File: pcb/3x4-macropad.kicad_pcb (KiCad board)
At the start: 2 copper layers, 83.1 x 78.9 mm, 47 parts, among them SW1 SW_Push, SW10 SW_Push, SW11 SW_Push, SW12 SW_Push, SW2 SW_Push, SW3 SW_Push, SW4 SW_Push, SW5 SW_Push, SW6 SW_Push, SW7 SW_Push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

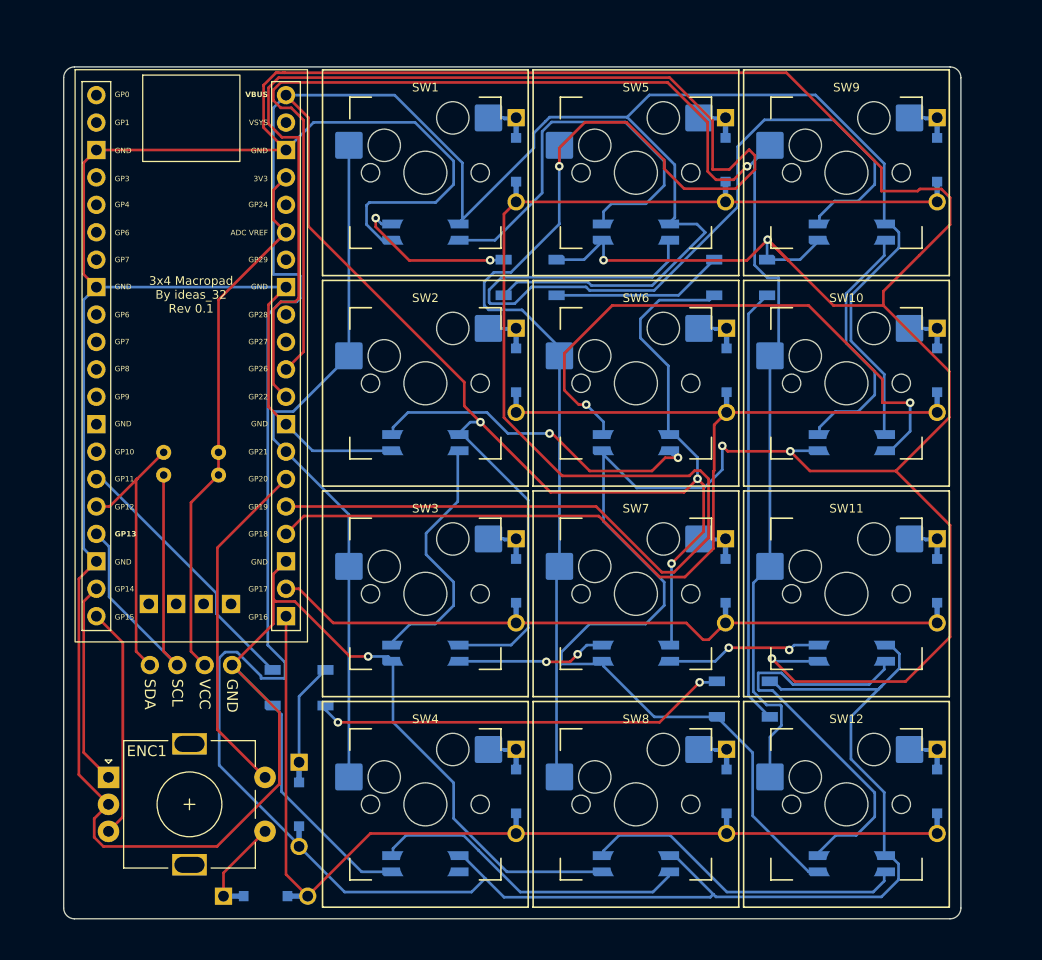
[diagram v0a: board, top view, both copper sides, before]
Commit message: Updated README.md and pcb with jlcpcb clearance requirements
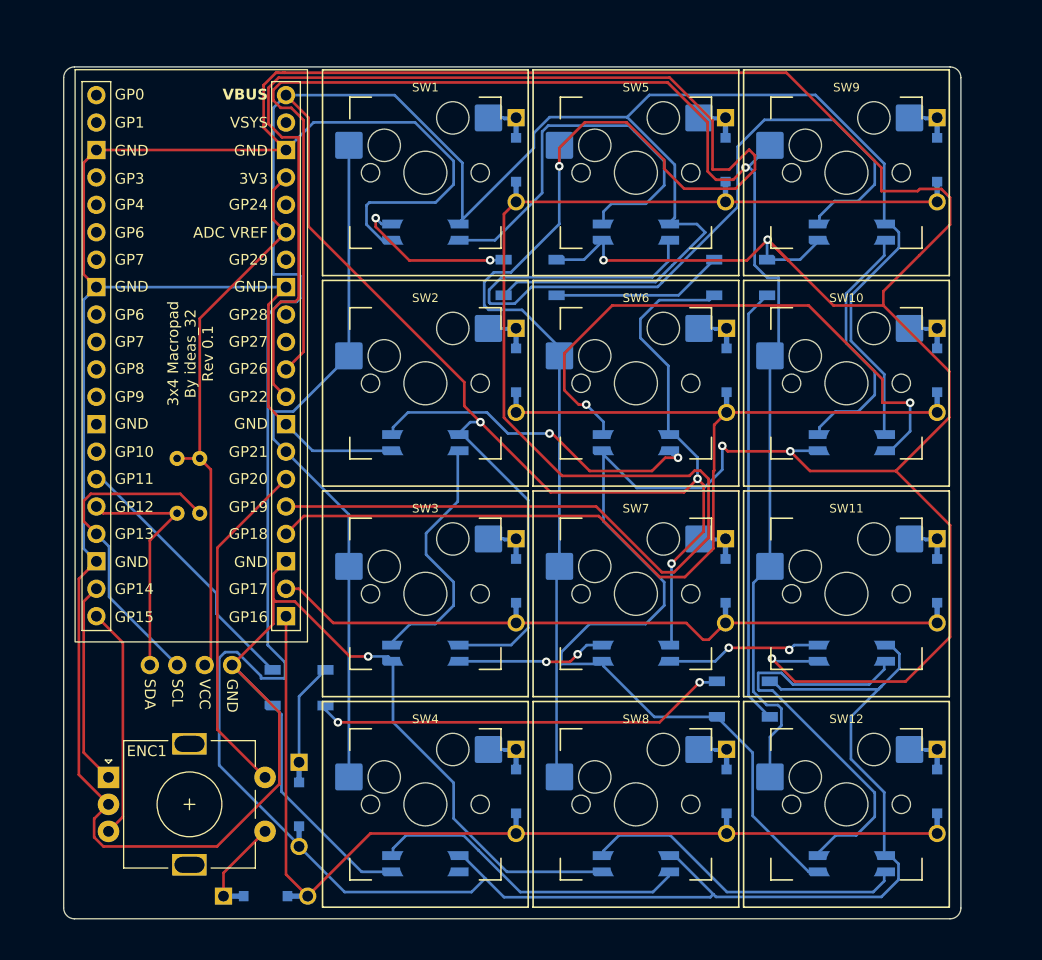
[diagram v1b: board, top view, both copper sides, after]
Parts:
- moved R1 5.77 mm to (138.0, 72.5), turned to 90 degrees
- moved R2 4.87 mm to (140.1, 72.5), turned to 90 degrees
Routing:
- net OLED_SDA: track 26.2 -> 22.8 mm
- net OLED_SCL: track 33.4 -> 30.6 mm
- net VCC: track 50.3 -> 52.2 mm
- net COL3: track 145.3 -> 143.9 mm

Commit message: stuff
- cleaned up routing
- changed per-key rgb footprint
- changed resistor footprint
- changed diode footprint to actually support sod123
- made power traces 0.5mm
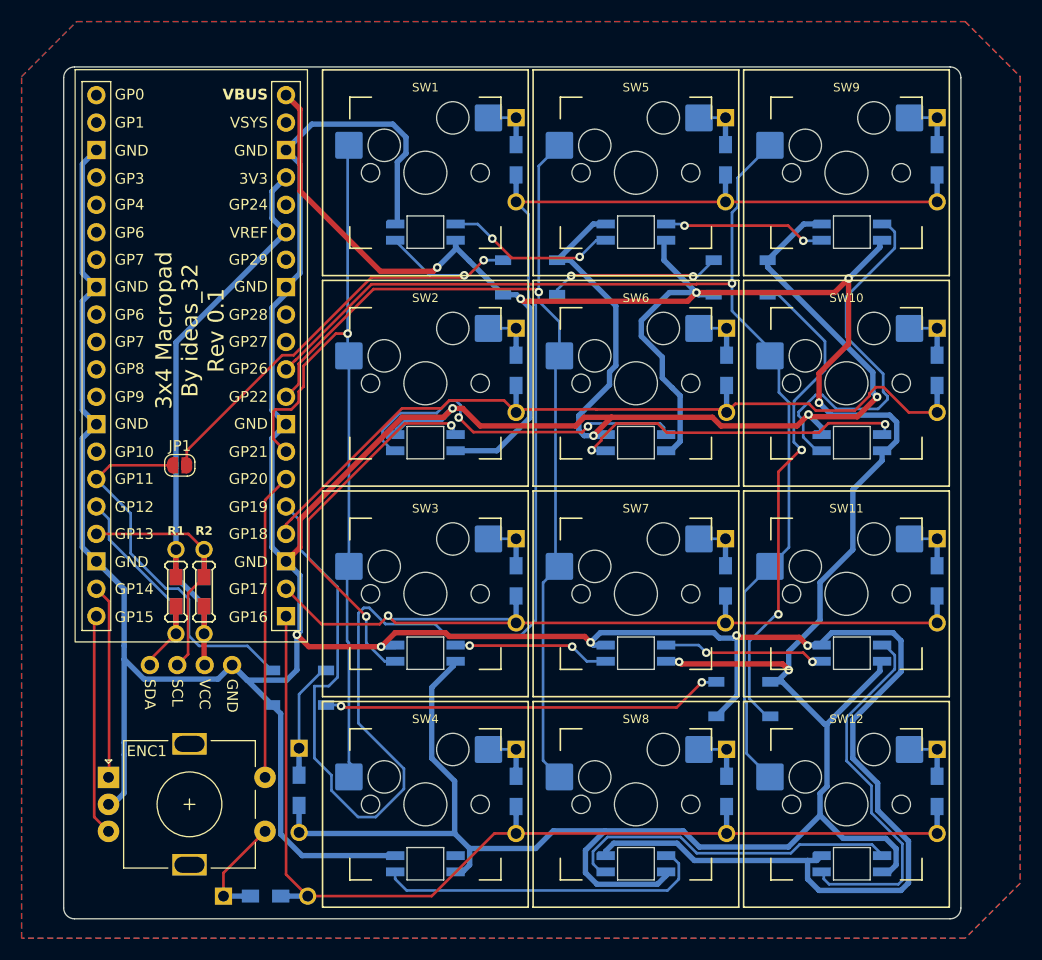
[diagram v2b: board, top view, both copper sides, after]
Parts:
- removed D18: D_Small, Keebio-Parts:Diode-dual
- added D14: 1N4148, Keebio-Parts:Diode-Hybrid-Back, B.Cu at (149.3, 98.2)
- added JP1: SolderJumper_2_Open, Jumper:SolderJumper-2_P1.3mm_Open_RoundedPad1.0x1.5mm, F.Cu at (138.2, 68.1)
- D1, D10, D11, D12, D13, D2, D3, D4, D5, D6, D7, D8, D9: value D_Small -> 1N4148; footprint Keebio-Parts:Diode-dual -> Keebio-Parts:Diode-Hybrid-Back
- LED1, LED10, LED11, LED12, LED2, LED3, LED4, LED5, LED6, LED7, LED8, LED9: footprint SK6812MINI-E:SK6812MINIE -> Keebio-Parts:SK6812-MINI-E
- LED13, LED14, LED15, LED16: footprint LED_SMD:LED_WS2812B_PLCC4_5.0x5.0mm_P3.2mm -> Keebio-Parts:WS2812B
- R1, R2: footprint Resistor_THT:R_Axial_DIN0204_L3.6mm_D1.6mm_P5.08mm_Horizontal -> Keebio-Parts:Resistor-Hybrid
- U1: value WeAct RP2040 Pico -> WeAct-RP2040-Pico
- moved R2 7.27 mm to (140.5, 79.8)
- moved R1 7.26 mm to (137.9, 79.8), turned to -90 degrees
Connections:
- U1 pad 13: unconnected-(U1-GND-Pad13) -> GND
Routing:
- net VBUS: track 467.7 -> 302.8 mm, vias 3 -> 7
- net GND: track 576.9 -> 444.5 mm, vias 6 -> 9
- net COL2: track 178.7 -> 89.4 mm
- net Net-(LED10-DIN): track 77.7 -> 15.4 mm, vias 0 -> 2
- net COL3: track 143.9 -> 107.6 mm
- net Net-(JP1-B): track 15.8 -> 45.4 mm
- net ROW1: track 101.4 -> 72.7 mm
- net ROW0: track 135.2 -> 158.4 mm
- net Net-(LED8-DIN): track 54.1 -> 31.3 mm
- net Net-(LED11-DIN): track 38.2 -> 16.3 mm, vias 0 -> 2
- net Net-(LED6-DIN): track 24.0 -> 35.1 mm, vias 0 -> 2
- net OLED_SCL: track 30.6 -> 19.7 mm
- net RGB: track 24.8 -> 35.4 mm
- net Net-(LED10-DOUT): track 23.9 -> 34.1 mm
- net ROW2: track 68.5 -> 78.6 mm, vias 0 -> 1
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- added copper zone on B.Cu, net GND
- added copper zone on F.Cu, net GND
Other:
- board text added: "COL0"
- board text added: "COL1"
- board text added: "COL2"
- board text added: "COL3"
- board text added: "ENC A"
- board text added: "ENC B"
- board text added: "GND"
- board text added: "Pins not labeled are unused"
- board text added: "RGB"
- board text added: "ROW0"
- board text added: "ROW1"
- board text added: "ROW2"
- board text added: "ROW3"
- board text added: "SCL"
- board text added: "SDA"
- board text added: "VBUS"
- board text added: "VCC"

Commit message: Updates and QOL
- changed revision silkscreen text
- removed silkscreen on diode pads
- updated readme.md
- ready for rev 0.2
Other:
- board text added: "3x4 Macropad By ideas_32 Rev 0.2"
- board text removed: "3x4 Macropad By ideas_32 Rev 0.1"

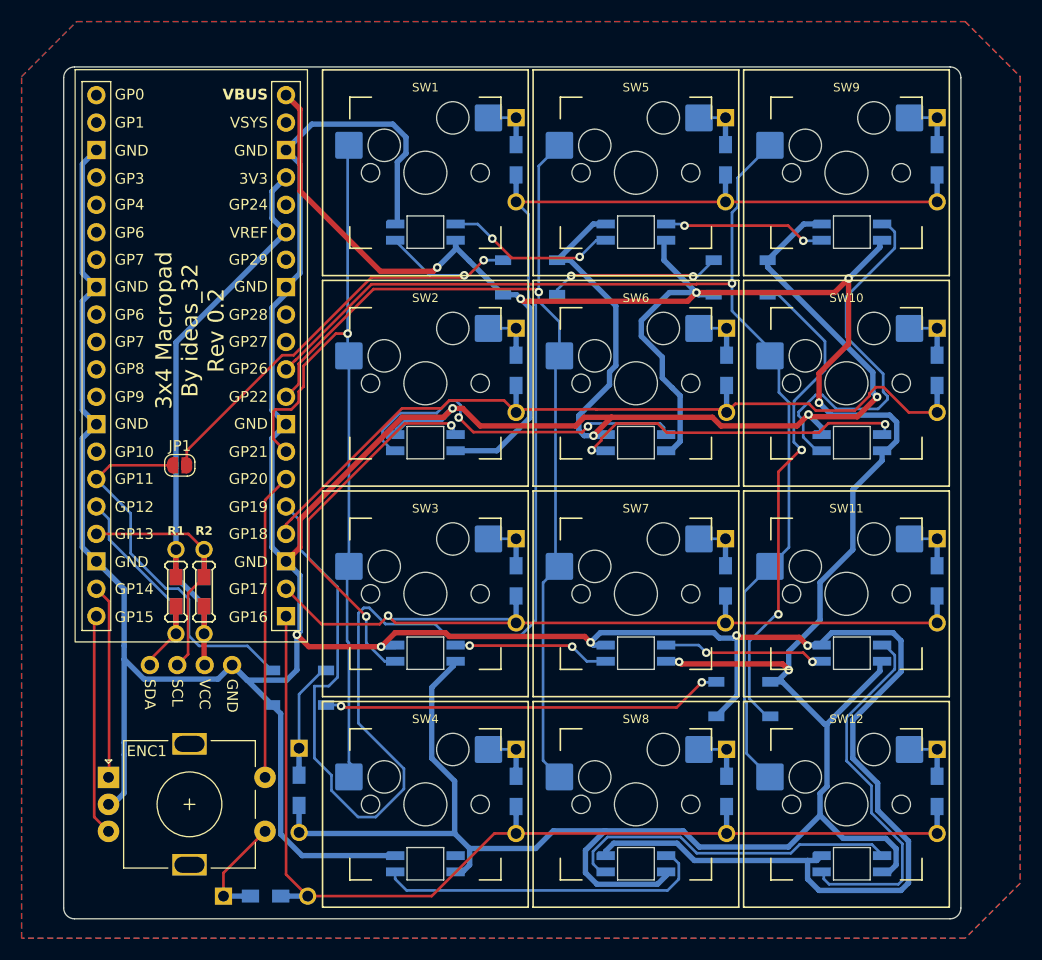
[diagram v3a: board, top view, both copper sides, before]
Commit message: flipped pi pico
- boot is still accessible because of cutout in board
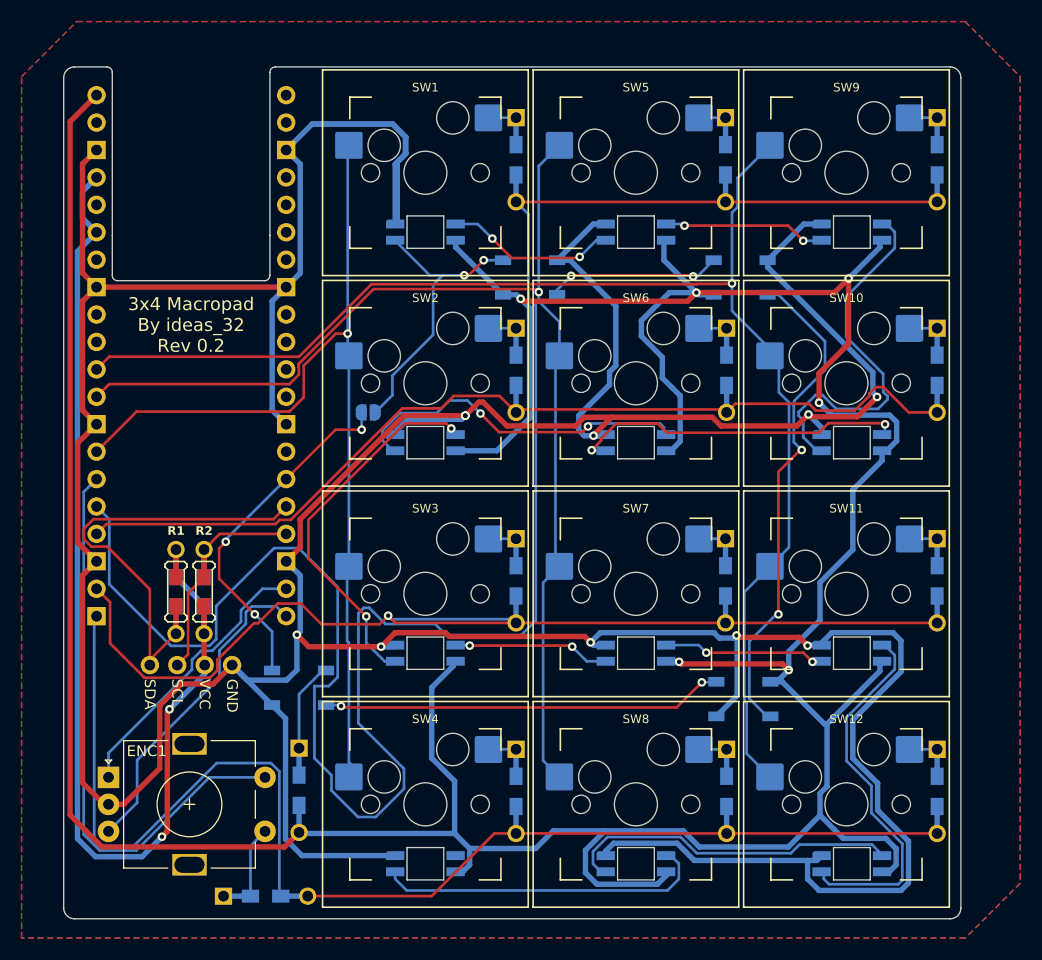
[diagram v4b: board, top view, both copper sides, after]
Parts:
- JP1, U1: moved to B.Cu
- moved JP1 18.1 mm to (155.7, 63.2)
- turned U1 to 180 degrees
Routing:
- net VBUS: track 302.8 -> 364.5 mm, vias 7 -> 6
- net VCC: track 46.5 -> 96.4 mm, vias 0 -> 2
- net GND: track 444.5 -> 476.4 mm, vias 9 -> 10
- net ROW0: track 158.4 -> 187.2 mm
- net ROW3: track 93.1 -> 119.0 mm
- net ROW2: track 78.6 -> 104.1 mm
- net COL0: track 28.4 -> 53.6 mm
- net OLED_SDA: track 16.2 -> 39.0 mm
- net Net-(JP1-B): track 45.4 -> 26.9 mm
- net COL3: track 107.6 -> 125.2 mm
- net ROW1: track 72.7 -> 90.0 mm
- net COL2: track 89.4 -> 106.4 mm
- net COL1: track 73.8 -> 87.3 mm
- net ENC_B: track 20.3 -> 29.9 mm
- net ENC_A: track 17.9 -> 26.2 mm
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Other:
- outline, holes or cut-outs redrawn
- board text removed: "COL0"
- board text removed: "COL1"
- board text removed: "COL2"
- board text removed: "COL3"
- board text removed: "ENC A"
- board text removed: "ENC B"
- board text removed: "Pins not labeled are unused"
- board text removed: "RGB"
- board text removed: "ROW0"
- board text removed: "ROW1"
- board text removed: "ROW2"
- board text removed: "ROW3"
- board text removed: "SCL"
- board text removed: "SDA"
- board text removed: "VBUS"
- board text removed: "VCC"

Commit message: V0.2 changed to gasket mount, added plate file, modified pcb to fix bugs
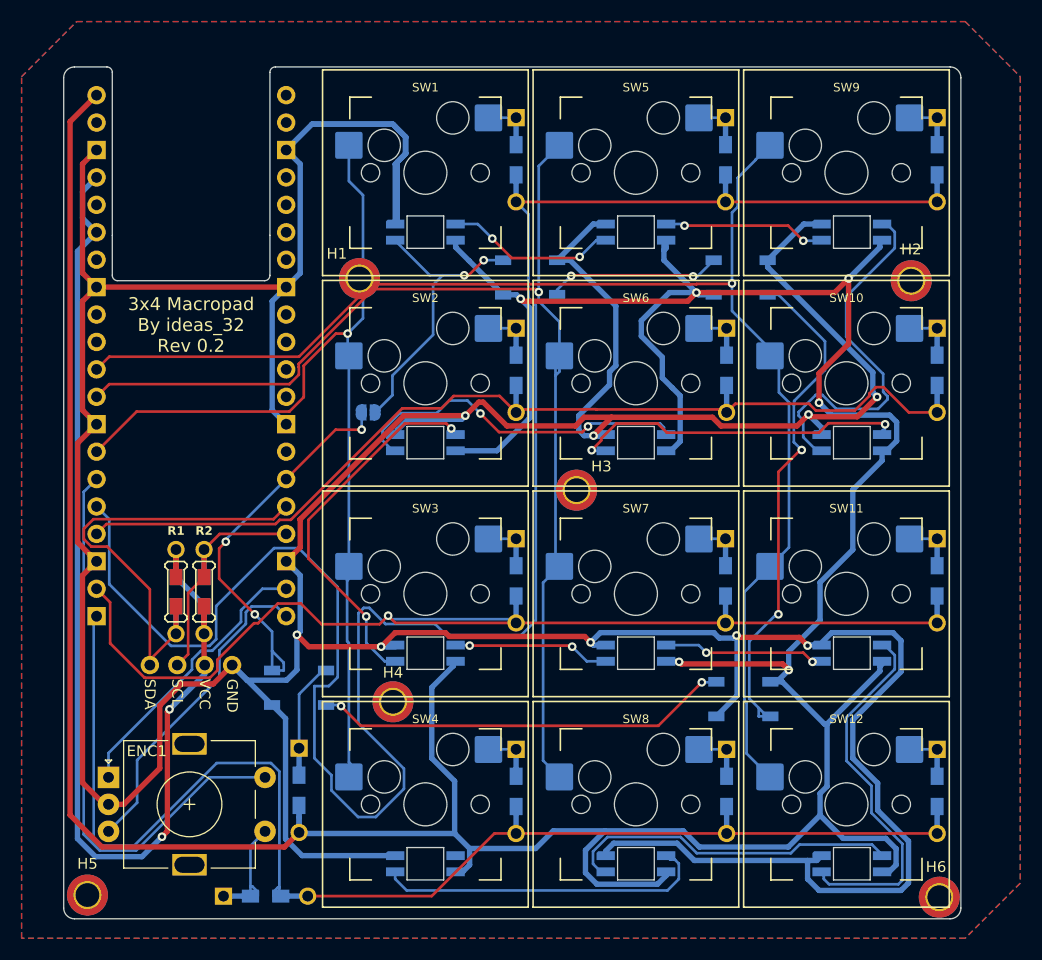
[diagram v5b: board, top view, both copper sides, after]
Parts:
- added H1: MountingHole, MountingHole:MountingHole_2.2mm_M2_DIN965_Pad_TopBottom, F.Cu at (154.9, 50.8)
- added H2: MountingHole, MountingHole:MountingHole_2.2mm_M2_DIN965_Pad_TopBottom, F.Cu at (206.0, 51.0)
- added H3: MountingHole, MountingHole:MountingHole_2.2mm_M2_DIN965_Pad_TopBottom, F.Cu at (175.0, 70.4)
- added H4: MountingHole, MountingHole:MountingHole_2.2mm_M2_DIN965_Pad_TopBottom, F.Cu at (158.0, 90.0)
- added H5: MountingHole, MountingHole:MountingHole_2.2mm_M2_DIN965_Pad_TopBottom, F.Cu at (129.7, 107.9)
- added H6: MountingHole, MountingHole:MountingHole_2.2mm_M2_DIN965_Pad_TopBottom, F.Cu at (208.6, 108.1)
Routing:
- net VCC: track 96.4 -> 106.8 mm
- net ROW3: track 119.0 -> 125.5 mm
- net VBUS: track 364.5 -> 370.2 mm
- net OLED_SDA: track 39.0 -> 44.1 mm
- net OLED_SCL: track 17.4 -> 22.5 mm
- net COL1: track 87.3 -> 92.2 mm
- net ROW1: track 90.0 -> 94.1 mm
- net RGB: track 32.8 -> 36.2 mm
- net ROW2: track 104.1 -> 107.4 mm
- net ROW0: track 187.2 -> 190.5 mm
- net Net-(D13-K): track 7.96 -> 11.0 mm
- net COL2: track 106.4 -> 109.1 mm
- net Net-(D14-K): track 8.21 -> 10.9 mm
- net Net-(D9-K): track 2.54 -> 5.07 mm
- net Net-(D6-K): track 2.54 -> 5.07 mm
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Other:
- board text removed: "GND"

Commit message: Initial release
Combination of many bugfixes, finally commiting the plate, and updating the silkscreen text
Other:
- board text added: "3x4 Macropad By ideas_32 Rev 1.0"
- board text removed: "3x4 Macropad By ideas_32 Rev 0.2"
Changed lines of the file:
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@@
   (gr_line (start 132.5 51) (end 146.1 51)
     (stroke (width 0.1) (type default)) (layer "Edge.Cuts"))
-  (gr_text "3x4 Macropad\nBy ideas_32\nRev 0.2" (at 139.3 55.1) (layer "B.SilkS")
+  (gr_text "3x4 Macropad\nBy ideas_32\nRev 1.0" (at 139.3 55.1) (layer "B.SilkS")
     (effects (font (size 1.2 1.2) (thickness 0.125)) (justify mirror))
   )
-  (gr_text "3x4 Macropad\nBy ideas_32\nRev 0.2" (at 139.3 55.1) (layer "F.SilkS")
+  (gr_text "3x4 Macropad\nBy ideas_32\nRev 1.0" (at 139.3 55.1) (layer "F.SilkS")
     (effects (font (size 1.2 1.2) (thickness 0.125)))
   )

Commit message: Fixed Bugs
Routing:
- net ROW0: track 190.5 -> 98.4 mm, vias 0 -> 1
- net GND: track 476.4 -> 435.4 mm, vias 9 -> 14
- net VBUS: track 370.2 -> 330.1 mm, vias 6 -> 12
- net VCC: track 106.8 -> 72.5 mm, vias 2 -> 1
- net OLED_SDA: track 44.1 -> 25.1 mm, vias 0 -> 1
- net COL0: track 53.6 -> 35.1 mm, vias 0 -> 1
- net ROW3: track 125.5 -> 107.2 mm
- net ROW2: track 107.4 -> 91.2 mm
- net COL1: track 92.2 -> 83.8 mm, vias 1 -> 2
- net Net-(LED10-DOUT): track 35.0 -> 28.1 mm
- net RGB: track 36.2 -> 29.9 mm, vias 3 -> 0
- net Net-(LED3-DIN): track 35.1 -> 29.8 mm
- net Net-(LED7-DIN): track 32.5 -> 27.5 mm, vias 2 -> 0
- net Net-(LED14-DIN): track 48.1 -> 43.9 mm
- net Net-(LED6-DIN): track 35.2 -> 31.6 mm
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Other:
- board text added: "JLCJLCJLCJLC"
